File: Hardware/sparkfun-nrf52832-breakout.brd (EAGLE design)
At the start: 17.8 x 52.1 mm, 48 parts, among them J5 CORTEX_DEBUGPTH, U1 AP2112K-3.3V, U2 NRF52832, Y1 32MHz, Y2 32.768kHz

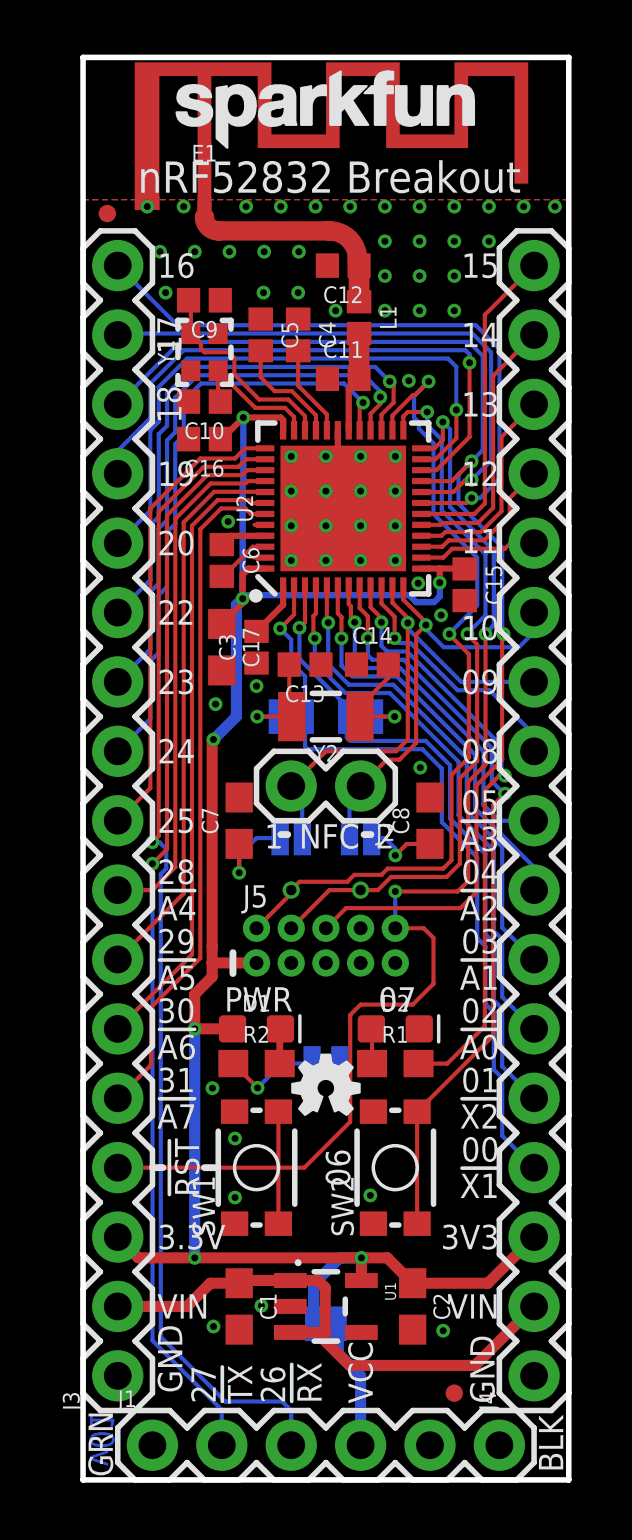
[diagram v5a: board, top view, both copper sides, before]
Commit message: Making SWD test points larger drill diameter.
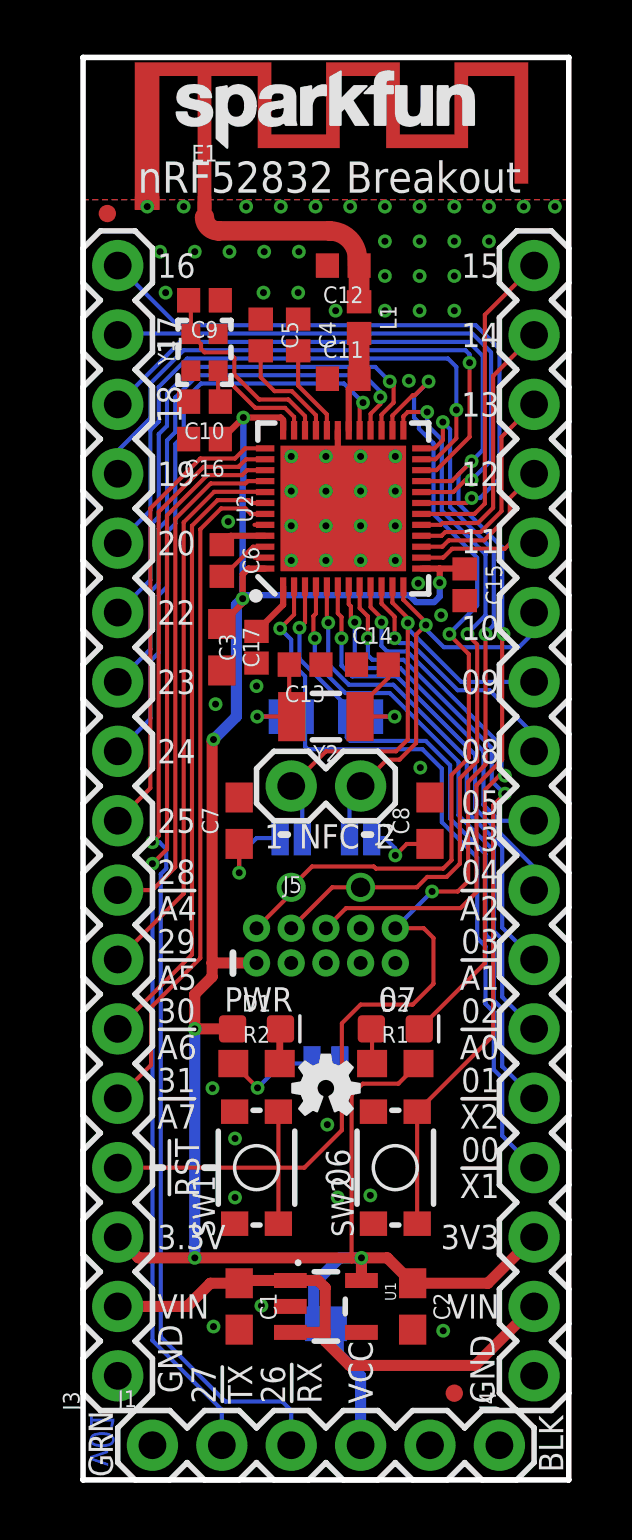
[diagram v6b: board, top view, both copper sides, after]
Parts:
- J5: device Pete_Connectors_Retired:2X5-PTH-1.27MM -> SparkFun-Connectors:2X5-PTH-1.27MM
- TP1, TP2: value (none) -> TEST-POINT3X4; device SparkFun-Connectors:TP_15TH -> SparkFun-Connectors:PAD.03X.04
- moved TP1 0.10 mm to (7.62, 21.7), flipped to the bottom
- moved TP2 0.10 mm to (10.2, 21.7), flipped to the bottom
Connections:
- net GND: no longer D2.C
- net P07: now also D2.C; no longer R1.2
- net VDD: now also R1.2
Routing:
- net VDD: track 71.8 -> 80.7 mm
- net P07: track 22.0 -> 20.1 mm
- net !RESET!: track 47.7 -> 46.9 mm
- net SWDIO: track 30.3 -> 30.7 mm, vias 2 -> 3
- net SWDCLK: vias 2 -> 3
- net GND: vias 61 -> 63
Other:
- board text added: "C"
- board text added: "D"
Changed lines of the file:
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@@
 <setting verticaltext="up"/>
 </settings>
-<grid distance="0.05" unitdist="inch" unit="inch" style="lines" multiple="1" display="yes" altdistance="0.005" altunitdist="inch" altunit="inch"/>
+<grid distance="0.001" unitdist="inch" unit="inch" style="lines" multiple="1" display="yes" altdistance="0.0005" altunitdist="inch" altunit="inch"/>
 <layers>
 <layer number="1" name="Top" color="4" fill="1" visible="yes" active="yes"/>
@@
 <text x="3.1623" y="3.175" size="0.889" layer="22" font="vector" ratio="15" rot="MR90" align="center-left">GND</text>
 <text x="15.24" y="8.89" size="0.889" layer="21" font="vector" ratio="15" align="center-right">3V3</text>
+<text x="6.9342" y="21.6916" size="0.889" layer="22" font="vector" ratio="15" rot="MR180" align="center-right">D</text>
+<text x="11.4554" y="21.6916" size="0.889" layer="22" font="vector" ratio="15" rot="MR180" align="center-right">C</text>
 </plain>
 <attributes>
@@
 <element name="J1" library="SparkFun-Connectors" package="1X06" value="" x="2.54" y="1.27"/>
 <element name="JP1" library="SparkFun-Jumpers" package="PAD-JUMPER-2-NO_YES_SILK" value="VDD-EN" x="8.89" y="5.715" rot="MR0"/>
-<element name="J5" library="Pete_Connectors_Retired" package="2X5-PTH-1.27MM" value="CORTEX_DEBUGPTH" x="8.89" y="19.558"/>
+<element name="J5" library="SparkFun-Connectors" package="2X5-PTH-1.27MM" value="CORTEX_DEBUGPTH" x="8.89" y="19.558"/>
 <element name="SW1" library="SparkFun-Electromechanical" package="TACTILE_SWITCH_SMD_4.6X2.8MM" value="" x="6.35" y="11.43" rot="R90">
 <attribute name="PROD_ID" value="SWCH-13065" x="6.35" y="11.43" size="1.778" layer="27" font="vector" ratio="15" rot="R90" display="off"/>
@@
 <element name="FD1" library="SparkFun-Aesthetics" package="FIDUCIAL-MICRO" value="FIDUCIALUFIDUCIAL" x="13.589" y="3.175"/>
 <element name="FD2" library="SparkFun-Aesthetics" package="FIDUCIAL-MICRO" value="FIDUCIALUFIDUCIAL" x="0.889" y="46.355"/>
-<element name="TP1" library="SparkFun-Connectors" package="TP_15TH" value="" x="7.62" y="21.59"/>
-<element name="TP2" library="SparkFun-Connectors" package="TP_15TH" value="" x="10.16" y="21.59"/>
+<element name="TP1" library="SparkFun-Connectors" package="PAD.03X.04" value="TEST-POINT3X4" x="7.62" y="21.6916" rot="MR0"/>
+<element name="TP2" library="SparkFun-Connectors" package="PAD.03X.04" value="TEST-POINT3X4" x="10.16" y="21.6916" rot="MR0"/>
 </elements>
 <signals>
@@
 <contactref element="C2" pad="2"/>
 <contactref element="C1" pad="2"/>
-<contactref element="D2" pad="C"/>
 <contactref element="SW1" pad="3"/>
 <contactref element="SW1" pad="4"/>
@@
 <via x="14.859" y="45.339" extent="1-16" drill="0.254"/>
 <contactref element="JP6" pad="1"/>
+<via x="9.3218" y="10.3378" extent="1-16" drill="0.254"/>
+<via x="8.9408" y="13.0048" extent="1-16" drill="0.254"/>
 </signal>
 <signal name="P00">
@@
 <wire x1="11.137" y1="8.128" x2="12.065" y2="7.2" width="0.4064" layer="1"/>
 <wire x1="10.1901" y1="7.3" x2="10.1901" y2="8.128" width="0.4064" layer="1"/>
-<wire x1="10.1901" y1="8.128" x2="4.0894" y2="8.128" width="0.4064" layer="1"/>
+<wire x1="10.1901" y1="8.128" x2="9.8298" y2="8.128" width="0.4064" layer="1"/>
+<wire x1="9.8298" y1="8.128" x2="4.0894" y2="8.128" width="0.4064" layer="1"/>
 <wire x1="4.0894" y1="8.128" x2="2.032" y2="8.128" width="0.4064" layer="1"/>
 <via x="4.0894" y="16.51" extent="1-16" drill="0.254"/>
@@
 <wire x1="4.0894" y1="17.78" x2="4.7244" y2="18.415" width="0.4064" layer="1"/>
 <wire x1="4.7244" y1="18.415" x2="4.7244" y2="18.923" width="0.4064" layer="1"/>
-<wire x1="4.7244" y1="19.5326" x2="4.7244" y2="27.051" width="0.4064" layer="1"/>
+<wire x1="4.7244" y1="18.923" x2="4.7244" y2="27.051" width="0.4064" layer="1"/>
 <wire x1="4.7244" y1="27.051" x2="4.7752" y2="27.1018" width="0.4064" layer="1"/>
 <via x="4.7752" y="27.1018" extent="1-16" drill="0.254"/>
@@
 <wire x1="9.398" y1="8.128" x2="8.44" y2="7.17" width="0.4064" layer="16"/>
 <wire x1="6.35" y1="18.923" x2="4.7244" y2="18.923" width="0.4064" layer="1"/>
-<wire x1="4.7244" y1="18.923" x2="4.7244" y2="19.5326" width="0.4064" layer="1"/>
+<contactref element="R1" pad="2"/>
+<wire x1="12.28" y1="15.24" x2="11.5434" y2="14.5034" width="0.1524" layer="1"/>
+<wire x1="11.5434" y1="14.5034" x2="10.2362" y2="14.5034" width="0.1524" layer="1"/>
+<wire x1="10.2362" y1="14.5034" x2="9.8298" y2="14.097" width="0.1524" layer="1"/>
+<wire x1="9.8298" y1="14.097" x2="9.8298" y2="8.128" width="0.1524" layer="1"/>
 </signal>
 <signal name="DEC1">
@@
 <wire x1="14.732" y1="30.988" x2="15.0368" y2="31.2928" width="0.1524" layer="16"/>
 <wire x1="14.732" y1="30.9626" x2="14.732" y2="26.1874" width="0.1524" layer="1"/>
-<via x="11.43" y="21.5392" extent="1-16" drill="0.254"/>
 <wire x1="12.827" y1="18.161" x2="12.827" y2="19.8374" width="0.1524" layer="1"/>
 <wire x1="12.827" y1="19.8374" x2="12.4714" y2="20.193" width="0.1524" layer="1"/>
 <wire x1="14.732" y1="26.1874" x2="14.097" y2="25.5524" width="0.1524" layer="1"/>
 <wire x1="14.097" y1="25.5524" x2="14.097" y2="21.9202" width="0.1524" layer="1"/>
-<wire x1="13.716" y1="21.5392" x2="11.43" y2="21.5392" width="0.1524" layer="1"/>
-<wire x1="8.1026" y1="11.43" x2="9.779" y2="13.1064" width="0.1524" layer="1"/>
-<wire x1="9.779" y1="13.1064" x2="9.779" y2="17.018" width="0.1524" layer="1"/>
-<wire x1="9.779" y1="17.018" x2="10.16" y2="17.399" width="0.1524" layer="1"/>
+<wire x1="8.1026" y1="11.43" x2="9.4742" y2="12.8016" width="0.1524" layer="1"/>
+<wire x1="9.4742" y1="12.8016" x2="9.4742" y2="16.7132" width="0.1524" layer="1"/>
+<wire x1="9.4742" y1="16.7132" x2="10.16" y2="17.399" width="0.1524" layer="1"/>
 <wire x1="10.16" y1="17.399" x2="12.065" y2="17.399" width="0.1524" layer="1"/>
 <wire x1="12.065" y1="17.399" x2="12.827" y2="18.161" width="0.1524" layer="1"/>
 <wire x1="14.097" y1="21.9202" x2="13.716" y2="21.5392" width="0.1524" layer="1"/>
-<wire x1="11.43" y1="21.5392" x2="11.43" y2="20.193" width="0.1524" layer="16"/>
 <wire x1="12.4714" y1="20.193" x2="11.43" y2="20.193" width="0.1524" layer="1"/>
+<wire x1="11.43" y1="20.193" x2="12.7762" y2="21.5392" width="0.1524" layer="16"/>
+<via x="12.7762" y="21.5392" extent="1-16" drill="0.254"/>
+<wire x1="12.7762" y1="21.5392" x2="13.716" y2="21.5392" width="0.1524" layer="1"/>
 </signal>
 <signal name="ANT">
@@
 <wire x1="11.1252" y1="30.3276" x2="11.8618" y2="30.3276" width="0.1524" layer="16"/>
 <wire x1="11.8618" y1="30.3276" x2="15.3162" y2="26.8732" width="0.1524" layer="16"/>
-<contactref element="R1" pad="2"/>
 <via x="15.4432" y="25.781" extent="1-16" drill="0.254"/>
 <wire x1="15.3162" y1="26.8732" x2="15.3162" y2="25.908" width="0.1524" layer="16"/>
 <wire x1="15.3162" y1="25.908" x2="15.4432" y2="25.781" width="0.1524" layer="16"/>
-<wire x1="14.7066" y1="16.6116" x2="14.7066" y2="25.2476" width="0.1524" layer="1"/>
+<wire x1="14.7066" y1="18.9096" x2="14.7066" y2="25.2476" width="0.1524" layer="1"/>
 <wire x1="15.4432" y1="25.781" x2="15.24" y2="25.781" width="0.1524" layer="1"/>
 <wire x1="15.24" y1="25.781" x2="14.7066" y2="25.2476" width="0.1524" layer="1"/>
-<wire x1="14.7066" y1="16.6116" x2="13.335" y2="15.24" width="0.1524" layer="1"/>
-<wire x1="13.335" y1="15.24" x2="12.28" y2="15.24" width="0.1524" layer="1"/>
+<contactref element="D2" pad="C"/>
+<wire x1="12.307" y1="16.51" x2="14.7066" y2="18.9096" width="0.1524" layer="1"/>
 </signal>
 <signal name="P06">
@@
 <contactref element="TP1" pad="P$1"/>
 <wire x1="13.4874" y1="22.6822" x2="13.1826" y2="22.3774" width="0.1524" layer="1"/>
-<wire x1="7.62" y1="21.59" x2="7.62" y2="21.463" width="0.1524" layer="1"/>
-<wire x1="7.62" y1="21.463" x2="6.35" y2="20.193" width="0.1524" layer="1"/>
-<wire x1="9.6774" y1="21.8948" x2="7.9248" y2="21.8948" width="0.1524" layer="1"/>
-<wire x1="7.9248" y1="21.8948" x2="7.62" y2="21.59" width="0.1524" layer="1"/>
-<wire x1="9.6774" y1="21.8948" x2="9.9314" y2="22.1488" width="0.1524" layer="1"/>
-<wire x1="9.9314" y1="22.1488" x2="10.922" y2="22.1488" width="0.1524" layer="1"/>
-<wire x1="10.922" y1="22.1488" x2="11.1506" y2="22.3774" width="0.1524" layer="1"/>
-<wire x1="11.1506" y1="22.3774" x2="13.1826" y2="22.3774" width="0.1524" layer="1"/>
+<wire x1="7.62" y1="21.6916" x2="7.62" y2="21.463" width="0.1524" layer="16"/>
+<via x="7.62" y="21.6916" extent="1-16" drill="0.7112"/>
+<wire x1="6.35" y1="20.193" x2="7.62" y2="21.463" width="0.1524" layer="1"/>
+<wire x1="7.62" y1="21.463" x2="7.62" y2="21.6916" width="0.1524" layer="1"/>
+<wire x1="8.382" y1="22.4536" x2="7.62" y2="21.6916" width="0.1524" layer="1"/>
+<wire x1="8.382" y1="22.4536" x2="10.6426" y2="22.4536" width="0.1524" layer="1"/>
+<wire x1="10.6426" y1="22.4536" x2="10.7188" y2="22.3774" width="0.1524" layer="1"/>
+<wire x1="10.7188" y1="22.3774" x2="13.1826" y2="22.3774" width="0.1524" layer="1"/>
 </signal>
 <signal name="SWDCLK">
@@
 <contactref element="TP2" pad="P$1"/>
 <wire x1="13.7922" y1="22.5552" x2="13.3096" y2="22.0726" width="0.1524" layer="1"/>
-<wire x1="9.017" y1="21.59" x2="7.62" y2="20.193" width="0.1524" layer="1"/>
-<wire x1="10.16" y1="21.59" x2="9.017" y2="21.59" width="0.1524" layer="1"/>
-<wire x1="10.16" y1="21.59" x2="10.795" y2="21.59" width="0.1524" layer="1"/>
-<wire x1="10.795" y1="21.59" x2="11.2776" y2="22.0726" width="0.1524" layer="1"/>
-<wire x1="11.2776" y1="22.0726" x2="13.3096" y2="22.0726" width="0.1524" layer="1"/>
+<wire x1="12.2174" y1="21.6916" x2="12.5984" y2="22.0726" width="0.1524" layer="1"/>
+<wire x1="12.5984" y1="22.0726" x2="13.3096" y2="22.0726" width="0.1524" layer="1"/>
+<via x="10.16" y="21.6916" extent="1-16" drill="0.7112"/>
+<wire x1="12.2174" y1="21.6916" x2="10.16" y2="21.6916" width="0.1524" layer="1"/>
+<wire x1="7.62" y1="20.193" x2="9.1186" y2="21.6916" width="0.1524" layer="1"/>
+<wire x1="9.1186" y1="21.6916" x2="10.16" y2="21.6916" width="0.1524" layer="1"/>
 </signal>
 <signal name="N$3">

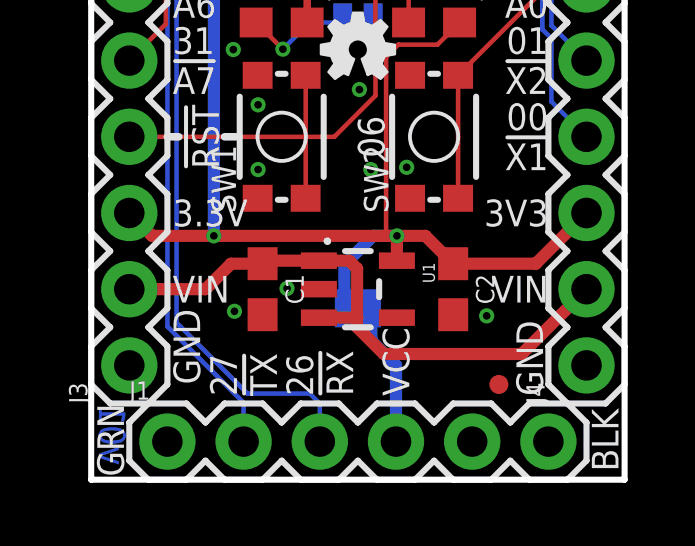
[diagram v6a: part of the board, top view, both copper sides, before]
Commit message: Defaulting JP1 to closed.
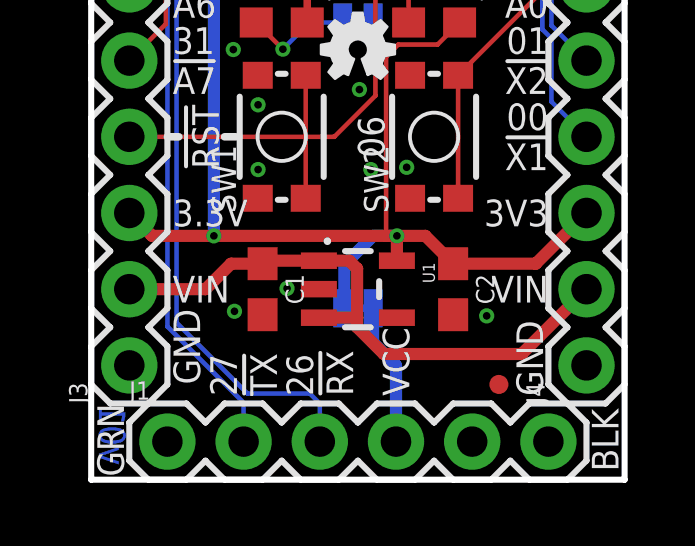
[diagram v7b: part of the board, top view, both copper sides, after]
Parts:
- JP1: device SparkFun-Jumpers:PAD-JUMPER-2-NO_YES_SILK -> SparkFun-Jumpers:SMT-JUMPER_2_NC_TRACE_SILK
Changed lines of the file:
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@@
 <setting verticaltext="up"/>
 </settings>
-<grid distance="0.001" unitdist="inch" unit="inch" style="lines" multiple="1" display="yes" altdistance="0.0005" altunitdist="inch" altunit="inch"/>
+<grid distance="0.05" unitdist="inch" unit="inch" style="lines" multiple="1" display="yes" altdistance="0.005" altunitdist="inch" altunit="inch"/>
 <layers>
 <layer number="1" name="Top" color="4" fill="1" visible="yes" active="yes"/>
@@
 <layer number="47" name="Measures" color="7" fill="1" visible="no" active="yes"/>
 <layer number="48" name="Document" color="7" fill="1" visible="no" active="yes"/>
-<layer number="49" name="Reference" color="7" fill="1" visible="yes" active="yes"/>
+<layer number="49" name="Reference" color="7" fill="1" visible="no" active="yes"/>
 <layer number="50" name="dxf" color="7" fill="1" visible="no" active="no"/>
 <layer number="51" name="tDocu" color="6" fill="1" visible="yes" active="yes"/>
@@
 </element>
 <element name="J1" library="SparkFun-Connectors" package="1X06" value="" x="2.54" y="1.27"/>
-<element name="JP1" library="SparkFun-Jumpers" package="PAD-JUMPER-2-NO_YES_SILK" value="VDD-EN" x="8.89" y="5.715" rot="MR0"/>
+<element name="JP1" library="SparkFun-Jumpers" package="SMT-JUMPER_2_NC_TRACE_SILK" value="VDD-EN" x="8.89" y="5.715" rot="MR0"/>
 <element name="J5" library="SparkFun-Connectors" package="2X5-PTH-1.27MM" value="CORTEX_DEBUGPTH" x="8.89" y="19.558"/>
 <element name="SW1" library="SparkFun-Electromechanical" package="TACTILE_SWITCH_SMD_4.6X2.8MM" value="" x="6.35" y="11.43" rot="R90">
@@
 <wire x1="5.842" y1="36.4744" x2="5.8674" y2="36.4998" width="0.2286" layer="16"/>
 <wire x1="5.8674" y1="36.4998" x2="5.8674" y2="38.8874" width="0.2286" layer="16"/>
-<wire x1="8.44" y1="5.715" x2="8.44" y2="7.17" width="0.4064" layer="16"/>
 <wire x1="10.1901" y1="8.128" x2="9.398" y2="8.128" width="0.4064" layer="16"/>
 <wire x1="9.398" y1="8.128" x2="8.44" y2="7.17" width="0.4064" layer="16"/>
@@
 <wire x1="10.2362" y1="14.5034" x2="9.8298" y2="14.097" width="0.1524" layer="1"/>
 <wire x1="9.8298" y1="14.097" x2="9.8298" y2="8.128" width="0.1524" layer="1"/>
+<wire x1="8.382" y1="5.715" x2="8.44" y2="5.773" width="0.4064" layer="16"/>
+<wire x1="8.44" y1="5.773" x2="8.44" y2="7.17" width="0.4064" layer="16"/>
 </signal>
 <signal name="DEC1">
@@
 <contactref element="J1" pad="4"/>
 <contactref element="JP1" pad="1"/>
-<wire x1="9.34" y1="5.715" x2="9.34" y2="4.63" width="0.4064" layer="16"/>
-<wire x1="9.34" y1="4.63" x2="10.16" y2="3.81" width="0.4064" layer="16"/>
 <wire x1="10.16" y1="3.81" x2="10.16" y2="1.27" width="0.4064" layer="16"/>
+<wire x1="10.16" y1="3.81" x2="9.398" y2="4.572" width="0.4064" layer="16"/>
+<wire x1="9.398" y1="4.572" x2="9.398" y2="5.715" width="0.4064" layer="16"/>
 </signal>
 <signal name="VIN">
